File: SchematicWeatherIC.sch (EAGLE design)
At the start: 25 parts, among them U1 ESP32-C6FH4, U2 MIC5365-3.3YC5-TR

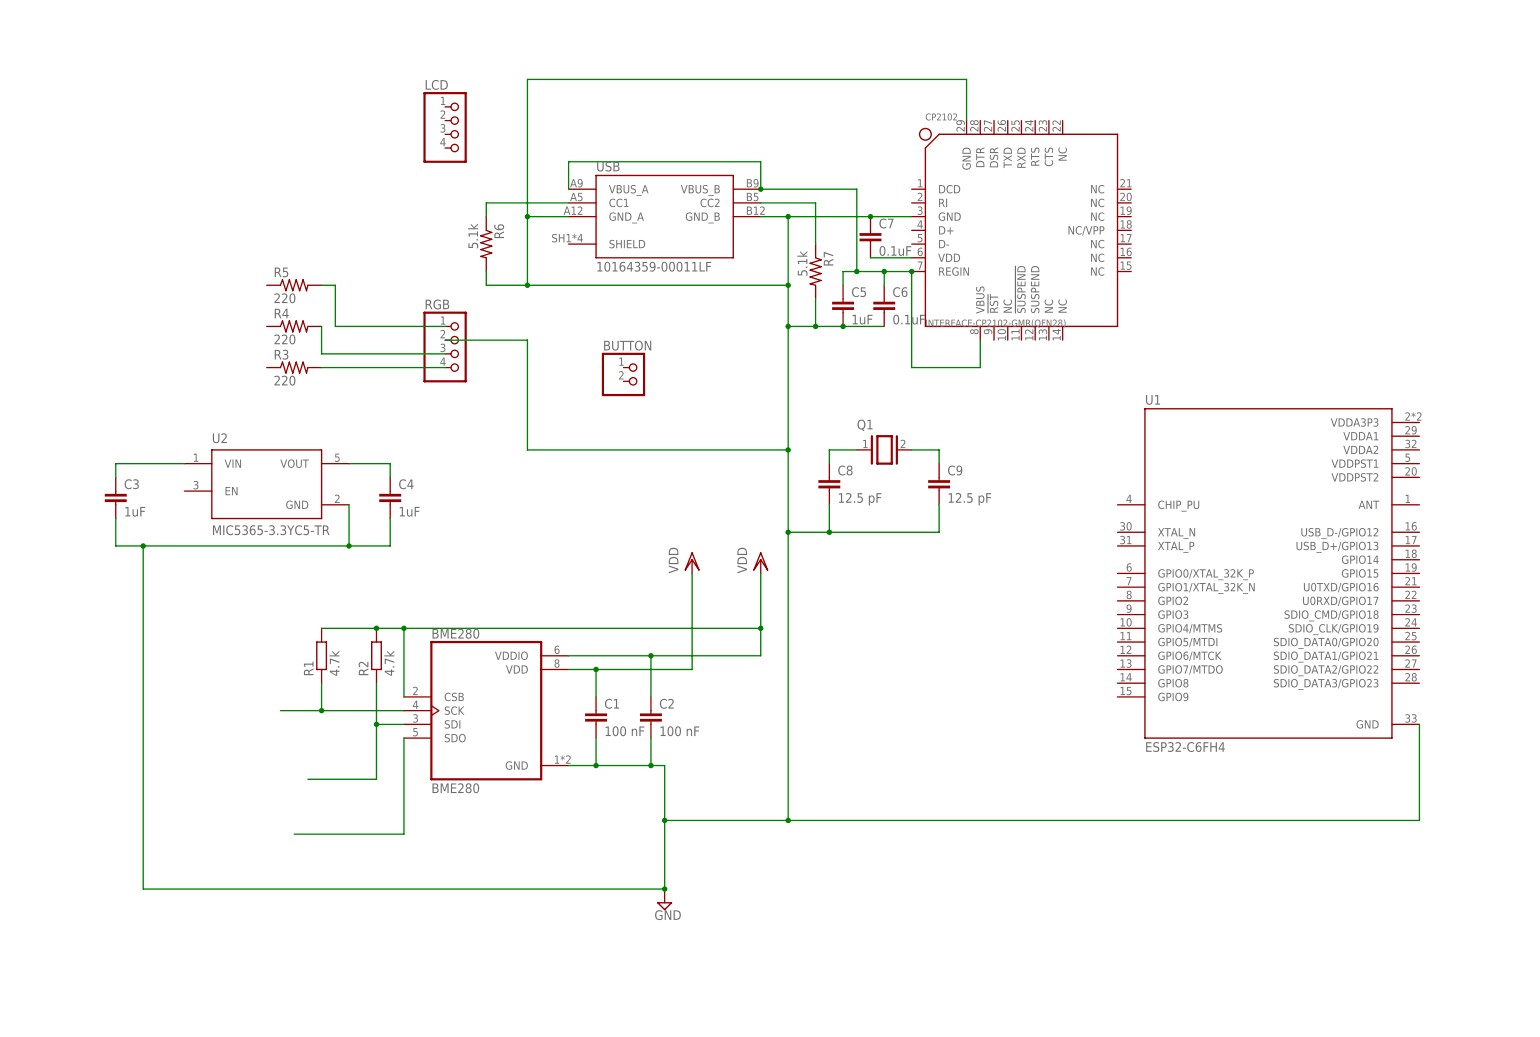
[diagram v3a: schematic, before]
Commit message: add lcd and some vdd connections
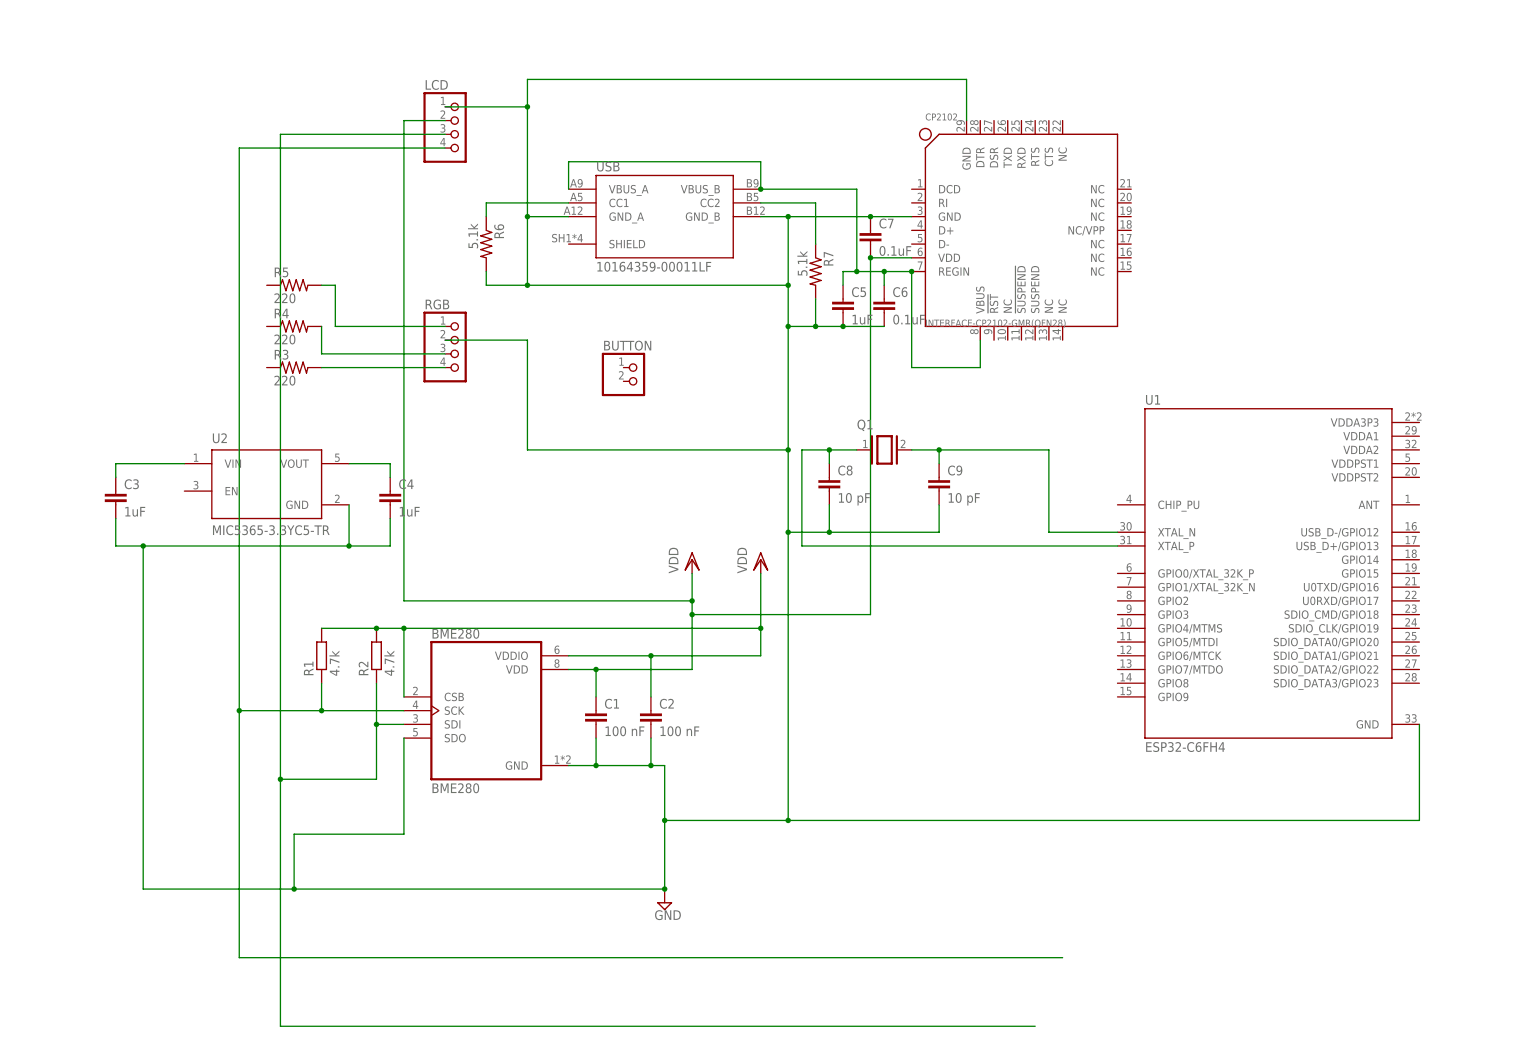
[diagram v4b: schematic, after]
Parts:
- C8, C9: value 12.5 pF -> 10 pF
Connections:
- removed net N$4: BME280.SDO
- removed net N$7: C7.2, CP2102.VDD
- net GND: now also BME280.SDO, LCD.1
- net N$1: now also LCD.4
- net N$11: now also U1.XTAL_P
- net N$15: now also U1.XTAL_N
- net N$3: now also LCD.3
- net VDD: now also C7.2, CP2102.VDD, LCD.2
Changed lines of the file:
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@@
 <part name="R7" library="rcl" library_urn="urn:adsk.eagle:library:334" deviceset="R-US_" device="VMTB60" package3d_urn="urn:adsk.eagle:package:26122/2" value="5.1k"/>
 <part name="Q1" library="special" library_urn="urn:adsk.eagle:library:367" deviceset="XTAL/S" device="" package3d_urn="urn:adsk.eagle:package:26647/2"/>
-<part name="C8" library="capacitor-wima" library_urn="urn:adsk.eagle:library:116" deviceset="C" device="5/3" package3d_urn="urn:adsk.eagle:package:5433/1" value="12.5 pF"/>
-<part name="C9" library="capacitor-wima" library_urn="urn:adsk.eagle:library:116" deviceset="C" device="5/3" package3d_urn="urn:adsk.eagle:package:5433/1" value="12.5 pF"/>
+<part name="C8" library="capacitor-wima" library_urn="urn:adsk.eagle:library:116" deviceset="C" device="5/3" package3d_urn="urn:adsk.eagle:package:5433/1" value="10 pF"/>
+<part name="C9" library="capacitor-wima" library_urn="urn:adsk.eagle:library:116" deviceset="C" device="5/3" package3d_urn="urn:adsk.eagle:package:5433/1" value="10 pF"/>
 </parts>
 <sheets>
@@
 <wire x1="73.66" y1="55.88" x2="78.74" y2="55.88" width="0.1524" layer="91"/>
 <wire x1="78.74" y1="55.88" x2="96.52" y2="55.88" width="0.1524" layer="91"/>
-<wire x1="96.52" y1="55.88" x2="96.52" y2="73.66" width="0.1524" layer="91"/>
+<wire x1="96.52" y1="55.88" x2="96.52" y2="66.04" width="0.1524" layer="91"/>
 <pinref part="C1" gate="G$1" pin="1"/>
+<wire x1="96.52" y1="66.04" x2="96.52" y2="68.58" width="0.1524" layer="91"/>
+<wire x1="96.52" y1="68.58" x2="96.52" y2="73.66" width="0.1524" layer="91"/>
 <wire x1="78.74" y1="50.8" x2="78.74" y2="55.88" width="0.1524" layer="91"/>
 <junction x="78.74" y="55.88"/>
+<pinref part="LCD" gate="A" pin="2"/>
+<wire x1="50.8" y1="157.48" x2="43.18" y2="157.48" width="0.1524" layer="91"/>
+<wire x1="43.18" y1="157.48" x2="43.18" y2="68.58" width="0.1524" layer="91"/>
+<wire x1="43.18" y1="68.58" x2="96.52" y2="68.58" width="0.1524" layer="91"/>
+<junction x="96.52" y="68.58"/>
+<pinref part="CP2102" gate="G$1" pin="VDD"/>
+<pinref part="C7" gate="G$1" pin="2"/>
+<wire x1="137.16" y1="132.08" x2="129.54" y2="132.08" width="0.1524" layer="91"/>
+<wire x1="129.54" y1="132.08" x2="129.54" y2="66.04" width="0.1524" layer="91"/>
+<wire x1="129.54" y1="66.04" x2="96.52" y2="66.04" width="0.1524" layer="91"/>
+<junction x="129.54" y="132.08"/>
+<junction x="96.52" y="66.04"/>
 </segment>
 <segment>
@@
 <wire x1="43.18" y1="48.26" x2="27.94" y2="48.26" width="0.1524" layer="91"/>
 <pinref part="R1" gate="G$1" pin="1"/>
-<wire x1="27.94" y1="48.26" x2="20.32" y2="48.26" width="0.1524" layer="91"/>
 <wire x1="27.94" y1="53.34" x2="27.94" y2="48.26" width="0.1524" layer="91"/>
 <junction x="27.94" y="48.26"/>
+<pinref part="LCD" gate="A" pin="4"/>
+<wire x1="50.8" y1="152.4" x2="12.7" y2="152.4" width="0.1524" layer="91"/>
+<wire x1="12.7" y1="152.4" x2="12.7" y2="48.26" width="0.1524" layer="91"/>
+<wire x1="12.7" y1="48.26" x2="27.94" y2="48.26" width="0.1524" layer="91"/>
+<wire x1="12.7" y1="48.26" x2="12.7" y2="2.54" width="0.1524" layer="91"/>
+<wire x1="12.7" y1="2.54" x2="165.1" y2="2.54" width="0.1524" layer="91"/>
+<junction x="12.7" y="48.26"/>
 </segment>
 </net>
@@
 <junction x="33.02" y="78.74"/>
 <wire x1="-5.08" y1="78.74" x2="-5.08" y2="15.24" width="0.1524" layer="91"/>
-<wire x1="-5.08" y1="15.24" x2="91.44" y2="15.24" width="0.1524" layer="91"/>
+<wire x1="-5.08" y1="15.24" x2="22.86" y2="15.24" width="0.1524" layer="91"/>
 <junction x="-5.08" y="78.74"/>
 <junction x="91.44" y="15.24"/>
 <pinref part="USB" gate="G$1" pin="GND_A"/>
+<wire x1="22.86" y1="15.24" x2="91.44" y2="15.24" width="0.1524" layer="91"/>
 <wire x1="73.66" y1="139.7" x2="66.04" y2="139.7" width="0.1524" layer="91"/>
 <wire x1="66.04" y1="139.7" x2="66.04" y2="127" width="0.1524" layer="91"/>
@@
 <wire x1="147.32" y1="157.48" x2="147.32" y2="165.1" width="0.1524" layer="91"/>
 <wire x1="147.32" y1="165.1" x2="66.04" y2="165.1" width="0.1524" layer="91"/>
-<wire x1="66.04" y1="165.1" x2="66.04" y2="139.7" width="0.1524" layer="91"/>
+<wire x1="66.04" y1="165.1" x2="66.04" y2="160.02" width="0.1524" layer="91"/>
 <junction x="66.04" y="139.7"/>
 <pinref part="CP2102" gate="G$1" pin="GND"/>
+<wire x1="66.04" y1="160.02" x2="66.04" y2="139.7" width="0.1524" layer="91"/>
 <wire x1="137.16" y1="139.7" x2="129.54" y2="139.7" width="0.1524" layer="91"/>
 <junction x="114.3" y="139.7"/>
@@
 <junction x="121.92" y="81.28"/>
 <junction x="114.3" y="81.28"/>
+<pinref part="LCD" gate="A" pin="1"/>
+<wire x1="50.8" y1="160.02" x2="66.04" y2="160.02" width="0.1524" layer="91"/>
+<junction x="66.04" y="160.02"/>
+<pinref part="BME280" gate="G$1" pin="SDO"/>
+<wire x1="43.18" y1="43.18" x2="43.18" y2="25.4" width="0.1524" layer="91"/>
+<wire x1="43.18" y1="25.4" x2="22.86" y2="25.4" width="0.1524" layer="91"/>
+<wire x1="22.86" y1="25.4" x2="22.86" y2="15.24" width="0.1524" layer="91"/>
+<junction x="22.86" y="15.24"/>
 </segment>
 </net>
@@
 <wire x1="43.18" y1="45.72" x2="38.1" y2="45.72" width="0.1524" layer="91"/>
 <wire x1="38.1" y1="45.72" x2="38.1" y2="35.56" width="0.1524" layer="91"/>
-<wire x1="38.1" y1="35.56" x2="25.4" y2="35.56" width="0.1524" layer="91"/>
+<wire x1="38.1" y1="35.56" x2="20.32" y2="35.56" width="0.1524" layer="91"/>
 <pinref part="R2" gate="G$1" pin="1"/>
 <wire x1="38.1" y1="53.34" x2="38.1" y2="45.72" width="0.1524" layer="91"/>
 <junction x="38.1" y="45.72"/>
-</segment>
-</net>
-<net name="N$4" class="0">
-<segment>
-<pinref part="BME280" gate="G$1" pin="SDO"/>
-<wire x1="43.18" y1="43.18" x2="43.18" y2="25.4" width="0.1524" layer="91"/>
-<wire x1="43.18" y1="25.4" x2="22.86" y2="25.4" width="0.1524" layer="91"/>
+<pinref part="LCD" gate="A" pin="3"/>
+<wire x1="50.8" y1="154.94" x2="20.32" y2="154.94" width="0.1524" layer="91"/>
+<wire x1="20.32" y1="154.94" x2="20.32" y2="35.56" width="0.1524" layer="91"/>
+<wire x1="20.32" y1="35.56" x2="20.32" y2="-10.16" width="0.1524" layer="91"/>
+<wire x1="20.32" y1="-10.16" x2="160.02" y2="-10.16" width="0.1524" layer="91"/>
+<junction x="20.32" y="35.56"/>
 </segment>
 </net>
@@
 </segment>
 </net>
-<net name="N$7" class="0">
-<segment>
-<pinref part="CP2102" gate="G$1" pin="VDD"/>
-<pinref part="C7" gate="G$1" pin="2"/>
-<wire x1="137.16" y1="132.08" x2="129.54" y2="132.08" width="0.1524" layer="91"/>
-</segment>
-</net>
 <net name="N$8" class="0">
 <segment>
@@
 <pinref part="C8" gate="G$1" pin="1"/>
 <wire x1="121.92" y1="96.52" x2="121.92" y2="93.98" width="0.1524" layer="91"/>
+<pinref part="U1" gate="G$1" pin="XTAL_P"/>
+<wire x1="175.26" y1="78.74" x2="116.84" y2="78.74" width="0.1524" layer="91"/>
+<wire x1="116.84" y1="78.74" x2="116.84" y2="96.52" width="0.1524" layer="91"/>
+<wire x1="116.84" y1="96.52" x2="121.92" y2="96.52" width="0.1524" layer="91"/>
+<junction x="121.92" y="96.52"/>
 </segment>
 </net>
@@
 <wire x1="142.24" y1="93.98" x2="142.24" y2="96.52" width="0.1524" layer="91"/>
 <wire x1="142.24" y1="96.52" x2="137.16" y2="96.52" width="0.1524" layer="91"/>
-</segment>
-</net>
+<wire x1="142.24" y1="96.52" x2="162.56" y2="96.52" width="0.1524" layer="91"/>
+<wire x1="162.56" y1="96.52" x2="162.56" y2="81.28" width="0.1524" layer="91"/>
+<junction x="142.24" y="96.52"/>
+<pinref part="U1" gate="G$1" pin="XTAL_N"/>
+<wire x1="162.56" y1="81.28" x2="175.26" y2="81.28" width="0.1524" layer="91"/>
+</segment>
+</net>

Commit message: all main connections on schematic complete
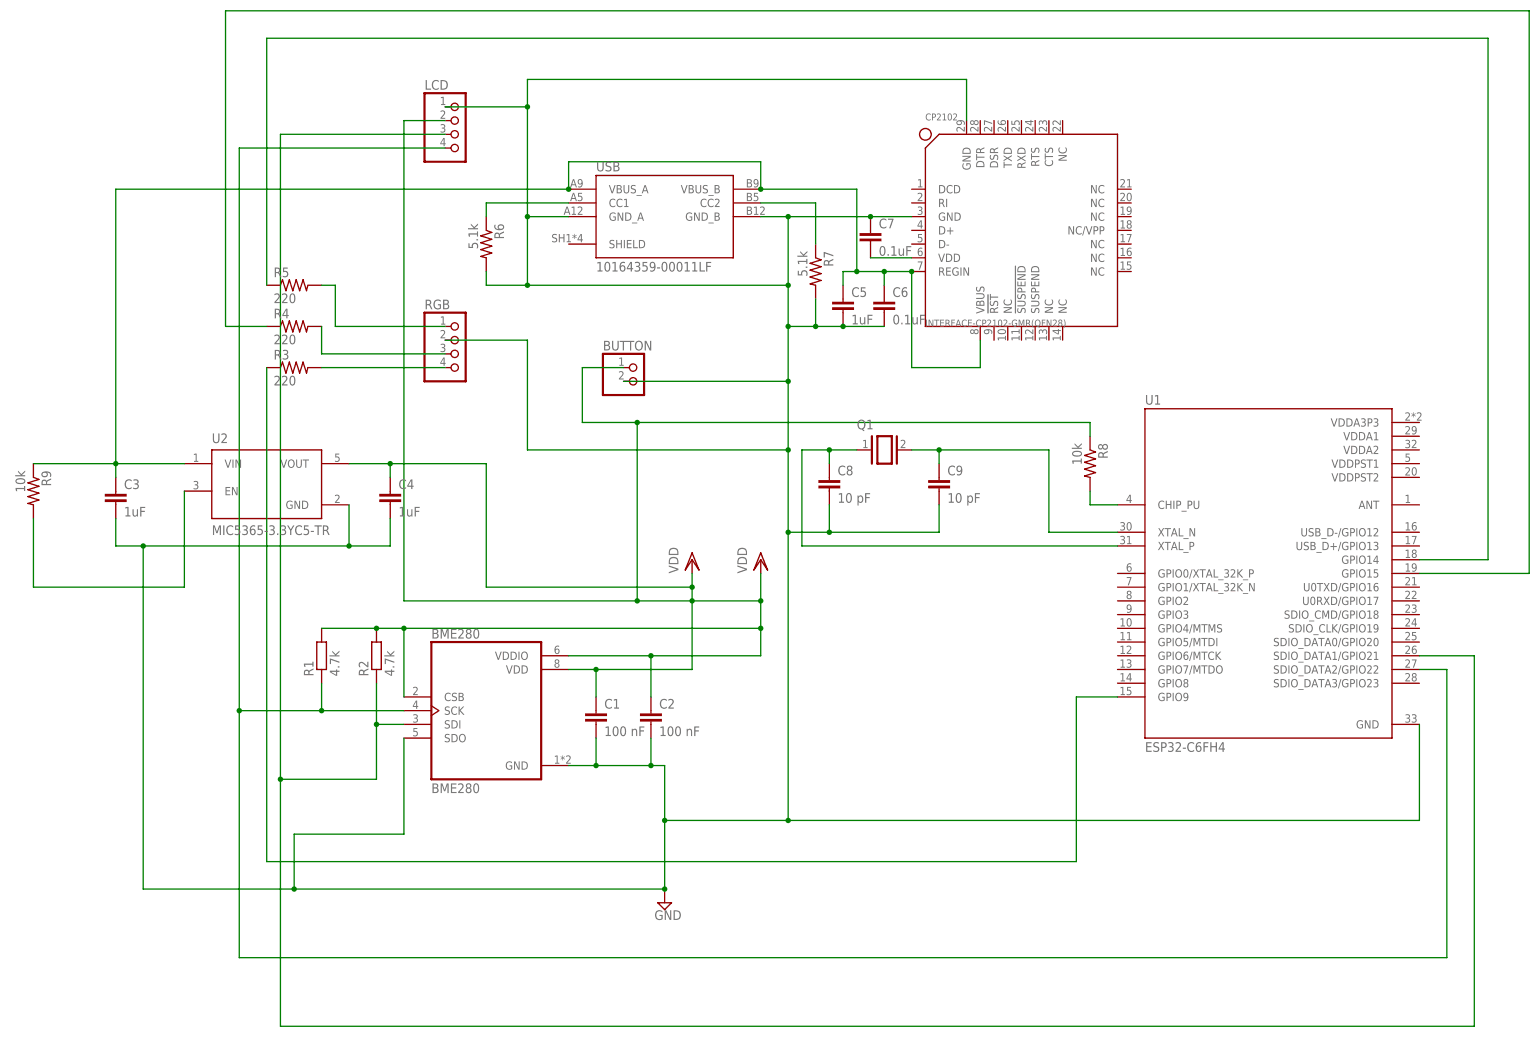
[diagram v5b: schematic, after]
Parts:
- added R8, R9: 10k, rcl:R-US_VMTB60
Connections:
- new net N$4: R5.1, U1.GPIO14
- new net N$7: R4.1, U1.GPIO15
- new net SCL: BME280.SCK, LCD.4, R1.1, U1.SDIO_DATA2/GPIO22
- new net SDA: BME280.SDI, LCD.3, R2.1, U1.SDIO_DATA1/GPIO21
- net GND: now also BUTTON.2
- net N$1: now also R3.1, U1.GPIO9; no longer BME280.SCK, LCD.4, R1.1
- net N$2: now also C5.1, C6.1, CP2102.REGIN, CP2102.VBUS, R9.1, USB.VBUS_A, USB.VBUS_B
- net N$3: now also R8.2, U1.CHIP_PU; no longer BME280.SDI, LCD.3, R2.1
- net N$5: now also C7.2, CP2102.VDD; no longer C4.1, U2.VOUT
- net N$6: now also R9.2, U2.EN; no longer C5.1, C6.1, CP2102.REGIN, CP2102.VBUS, USB.VBUS_A, USB.VBUS_B
- net VDD: now also BUTTON.1, C4.1, R8.1, U2.VOUT; no longer C7.2, CP2102.VDD
